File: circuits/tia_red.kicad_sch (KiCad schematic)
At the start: 11 parts, among them U2 OPA380AID

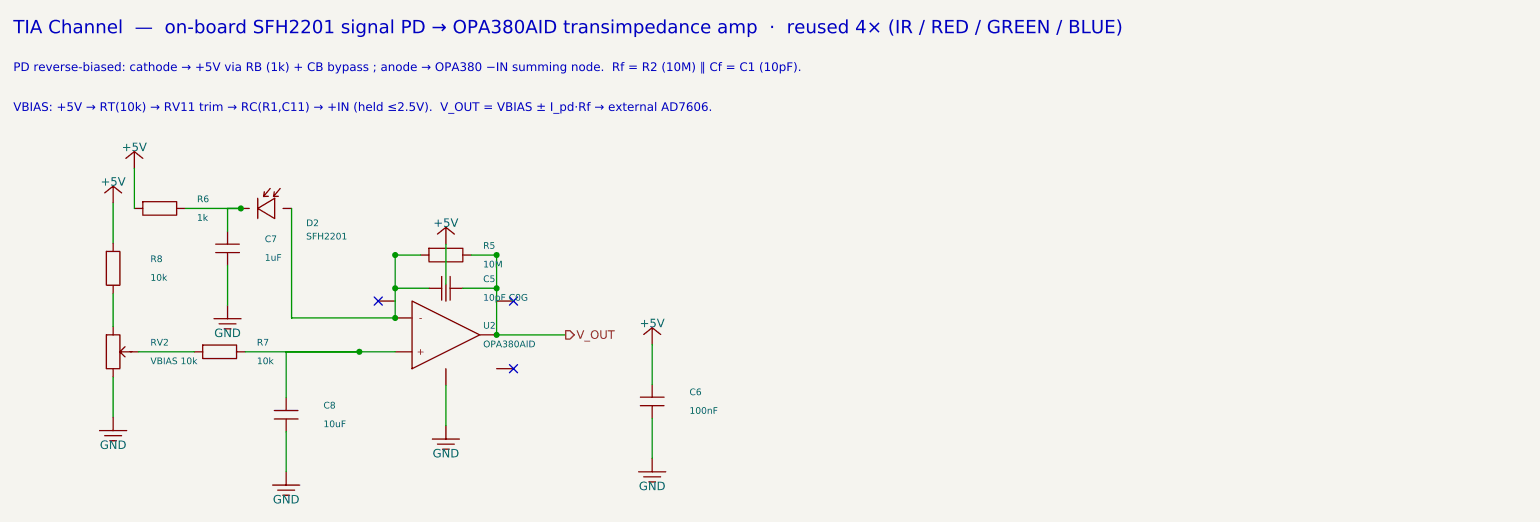
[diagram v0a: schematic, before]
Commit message: fix(circuits): import mcu sheet and laser footprints
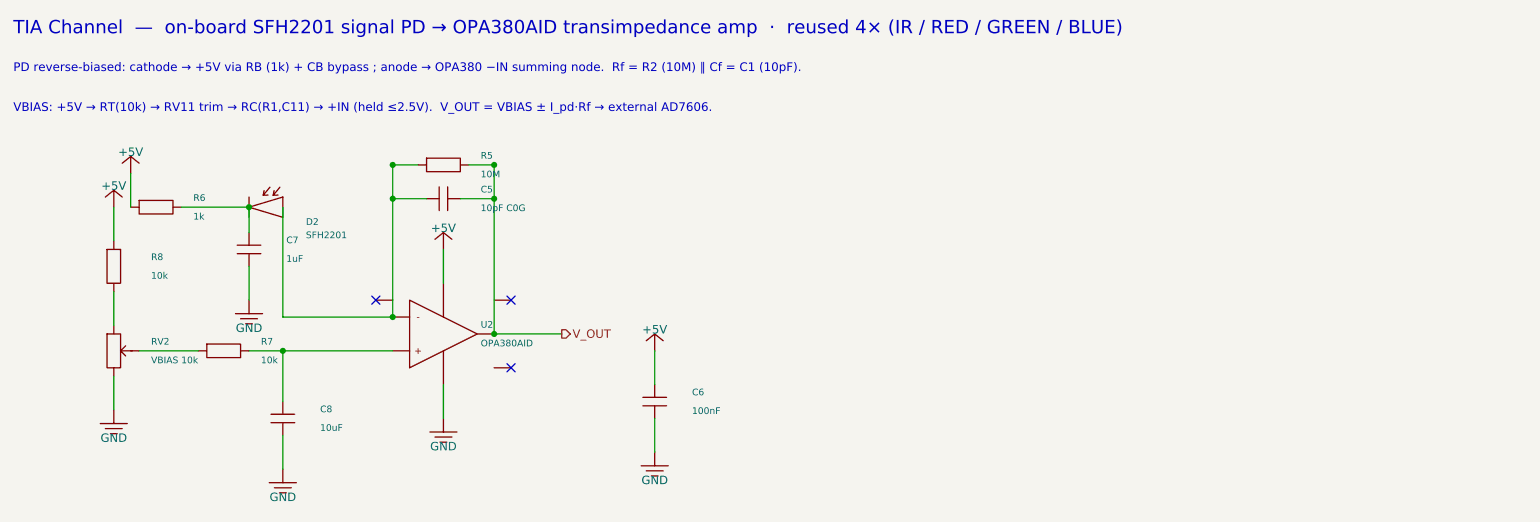
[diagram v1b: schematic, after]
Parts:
- C6: LCSC C1525 -> C83056; Part Number CL05B104KO5NNNC -> 0402B104K160CT
- C7: LCSC C52923 -> C7472946; Part Number CL05A105KA5NQNC -> HGC0402R5105K250NTEJ
- C8: LCSC C15850 -> C318691; Part Number CL21A106KAYNNNE -> CL21A106KAYNNNG
- R5: LCSC C57129 -> C844730; Part Number 0603WAF1005T5E -> CRCW060310M0FKEA
- R6: LCSC C21190 -> C2907002; Part Number 0603WAF1001T5E -> FRC0603F1001TS
- R7, R8: LCSC C269701 -> C844918; Part Number 0603WAF1002T5E -> CRCW060310K0FKEA

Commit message: save laser controller schematic and layout state
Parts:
- removed D2: SFH2201, OptoDevice:Osram_SFH2201, symbol viv:PHOTODIODE
- removed R5: 10M, Resistor_SMD:R_0603_1608Metric_Pad0.98x0.95mm_HandSolder, symbol viv:R_H
- removed RV2: VBIAS 10k, Potentiometer_SMD:Potentiometer_Bourns_3224W_Vertical, symbol viv:POT_V
- added C5: 10pF C0G, Capacitor_SMD:C_0603_1608Metric_Pad1.08x0.95mm_HandSolder, symbol viv:C_H
- added R7: 10k, Resistor_SMD:R_0603_1608Metric_Pad0.98x0.95mm_HandSolder, symbol viv:R_H
- added U2: OPA380AID, Package_SO:SOIC-8_3.9x4.9mm_P1.27mm, symbol viv:OPA_N
- C7: renamed from U2; value OPA380AID -> 1uF; footprint Package_SO:SOIC-8_3.9x4.9mm_P1.27mm -> Capacitor_SMD:C_0402_1005Metric_Pad0.74x0.62mm_HandSolder; symbol viv:OPA_N -> viv:C_V; LCSC C201677 -> C7472946; Part Number OPA380AID -> HGC0402R5105K250NTEJ
- D2: renamed from R6; value 1k -> SFH2201; footprint Resistor_SMD:R_0603_1608Metric_Pad0.98x0.95mm_HandSolder -> OptoDevice:Osram_SFH2201; symbol viv:R_H -> viv:PHOTODIODE; LCSC C2907002 -> C2900216; Part Number FRC0603F1001TS -> SFH2201
- R6: renamed from C7; value 1uF -> 1k; footprint Capacitor_SMD:C_0402_1005Metric_Pad0.74x0.62mm_HandSolder -> Resistor_SMD:R_0603_1608Metric_Pad0.98x0.95mm_HandSolder; symbol viv:C_V -> viv:R_H; LCSC C7472946 -> C2907002; Part Number HGC0402R5105K250NTEJ -> FRC0603F1001TS
- RV2: renamed from R7; value 10k -> VBIAS 10k; footprint Resistor_SMD:R_0603_1608Metric_Pad0.98x0.95mm_HandSolder -> Potentiometer_SMD:Potentiometer_Bourns_3224W_Vertical; symbol viv:R_H -> viv:POT_V; LCSC C844918 -> C81348; Part Number CRCW060310K0FKEA -> 3224W-1-103E
- RV6: renamed from C5; value 10pF C0G -> RF 2M; footprint Capacitor_SMD:C_0603_1608Metric_Pad1.08x0.95mm_HandSolder -> Potentiometer_SMD:Potentiometer_Bourns_3224W_Vertical; symbol viv:C_H -> viv:POT_H; LCSC C106245 -> C116323; Part Number CC0603JRNPO9BN100 -> 3224W-1-205E
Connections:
- net +5V: now also R6.1, U2.7 (V+); no longer C7.7 (V+), D2.1
- net GND: now also C7.2, RV2.3, U2.4 (V-); no longer C7.4 (V-), R6.2
- net V_OUT: now also RV6.3, C5.2, U2.6; no longer C7.6
- net at D2.2 (A): now also RV6.1, C5.1, U2.2 (-); no longer R6.1
- net at C7.1: now also D2.1 (K), R6.2
- net at R8.2: now also RV2.1
- new net: C8.1, R7.2, U2.3 (+)
- new net: R7.1, RV2.2 (W)
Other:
- note added: "PD reverse-biased: cathode → +5V via RB (1k) + CB bypass ; anode → OPA380 −IN summing node. Rf = RVFB (2M trim) ∥ Cf = C1 (10pF)."
- note added: "VBIAS: +5V → RT(10k) → RV11 trim → RC(R1,C11) → +IN (held ≤2.5V). V_OUT = VBIAS ± I_pd·Rf → on-board AD7606-4."
- note removed: "PD reverse-biased: cathode → +5V via RB (1k) + CB bypass ; anode → OPA380 −IN summing node. Rf = R2 (10M) ∥ Cf = C1 (10pF)."
- note removed: "VBIAS: +5V → RT(10k) → RV11 trim → RC(R1,C11) → +IN (held ≤2.5V). V_OUT = VBIAS ± I_pd·Rf → external AD7606."
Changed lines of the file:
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@@
     )
   )
-  (symbol (lib_id "viv:R_H") (at 214.63 124.46 0) (unit 1)
-    (in_bom yes) (on_board yes) (dnp no)
-    (property "Reference" "R5" (at 220.23 123.06 0) (effects (font (size 1.0 1.0)) (justify left)))
-    (property "Value" "10M" (at 220.23 125.86 0) (effects (font (size 1.0 1.0)) (justify left)))
-    (property "Footprint" "Resistor_SMD:R_0603_1608Metric_Pad0.98x0.95mm_HandSolder" (at 214.63 124.46 0) (effects (font (size 1.0 1.0)) hide))
+  (symbol (lib_id "viv:POT_H") (at 214.63 124.46 0) (unit 1)
+    (in_bom yes) (on_board yes) (dnp no)
+    (property "Reference" "RV6" (at 220.23 123.06 0) (effects (font (size 1.0 1.0)) (justify left)))
+    (property "Value" "RF 2M" (at 220.23 125.86 0) (effects (font (size 1.0 1.0)) (justify left)))
+    (property "Footprint" "Potentiometer_SMD:Potentiometer_Bourns_3224W_Vertical" (at 214.63 124.46 0) (effects (font (size 1.0 1.0)) hide))
     (property "Datasheet" "" (at 214.63 124.46 0) (effects (font (size 1.0 1.0)) hide))
-    (property "Part Number" "CRCW060310M0FKEA" (at 214.63 124.46 0) (effects (font (size 1.0 1.0)) hide))
-    (property "LCSC" "C844730" (at 214.63 124.46 0) (effects (font (size 1.0 1.0)) hide))
-    (pin "1")
-    (pin "2")
-    (instances
-      (project "laser_controller"
-        (path "/c1d2e3f4-6000-4000-a000-000000000001" (reference "R5") (unit 1))
+    (property "Part Number" "3224W-1-205E" (at 214.63 124.46 0) (effects (font (size 1.0 1.0)) hide))
+    (property "LCSC" "C116323" (at 214.63 124.46 0) (effects (font (size 1.0 1.0)) hide))
+    (pin "1")
+    (pin "2")
+    (pin "3")
+    (instances
+      (project "laser_controller"
+        (path "/c1d2e3f4-6000-4000-a000-000000000001" (reference "RV6") (unit 1))
       )
     )
@@
   (wire (pts (xy 210.82 124.46) (xy 207.01 124.46)) (stroke (width 0) (type default)))
   (wire (pts (xy 218.44 124.46) (xy 222.25 124.46)) (stroke (width 0) (type default)))
+  (wire (pts (xy 214.63 120.65) (xy 222.25 120.65)) (stroke (width 0) (type default)))
+  (wire (pts (xy 222.25 120.65) (xy 222.25 124.46)) (stroke (width 0) (type default)))
   (wire (pts (xy 212.09 129.54) (xy 207.01 129.54)) (stroke (width 0) (type default)))
   (wire (pts (xy 217.17 129.54) (xy 222.25 129.54)) (stroke (width 0) (type default)))
@@
   (hierarchical_label "V_OUT" (shape output) (at 232.41 149.86 0) (effects (font (size 1.27 1.27)) (justify left)))
   (text "TIA Channel  —  on-board SFH2201 signal PD → OPA380AID transimpedance amp  ·  reused 4× (IR / RED / GREEN / BLUE)" (at 150 104 0) (effects (font (size 2.0 2.0)) (justify left)))
-  (text "PD reverse-biased: cathode → +5V via RB (1k) + CB bypass ; anode → OPA380 −IN summing node.  Rf = R2 (10M) ∥ Cf = C1 (10pF)." (at 150 110 0) (effects (font (size 1.3 1.3)) (justify left)))
-  (text "VBIAS: +5V → RT(10k) → RV11 trim → RC(R1,C11) → +IN (held ≤2.5V).  V_OUT = VBIAS ± I_pd·Rf → external AD7606." (at 150 116 0) (effects (font (size 1.3 1.3)) (justify left)))
+  (text "PD reverse-biased: cathode → +5V via RB (1k) + CB bypass ; anode → OPA380 −IN summing node.  Rf = RVFB (2M trim) ∥ Cf = C1 (10pF)." (at 150 110 0) (effects (font (size 1.3 1.3)) (justify left)))
+  (text "VBIAS: +5V → RT(10k) → RV11 trim → RC(R1,C11) → +IN (held ≤2.5V).  V_OUT = VBIAS ± I_pd·Rf → on-board AD7606-4." (at 150 116 0) (effects (font (size 1.3 1.3)) (justify left)))
   (sheet_instances
     (path "/" (page "1"))
